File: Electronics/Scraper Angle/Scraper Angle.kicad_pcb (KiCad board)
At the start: 2 copper layers, 43 x 51 mm, 20 parts, among them J1 TERM, J12 SENSOR, J14 CAN BUS, J2 CAN BUS, J3 Conn_01x02, J4 Conn_01x02, J5 Conn_01x02, U1 TJA1462ATK-0Z, U2 PESD2CANFD24V-TR, U3 TEENSY 4.0

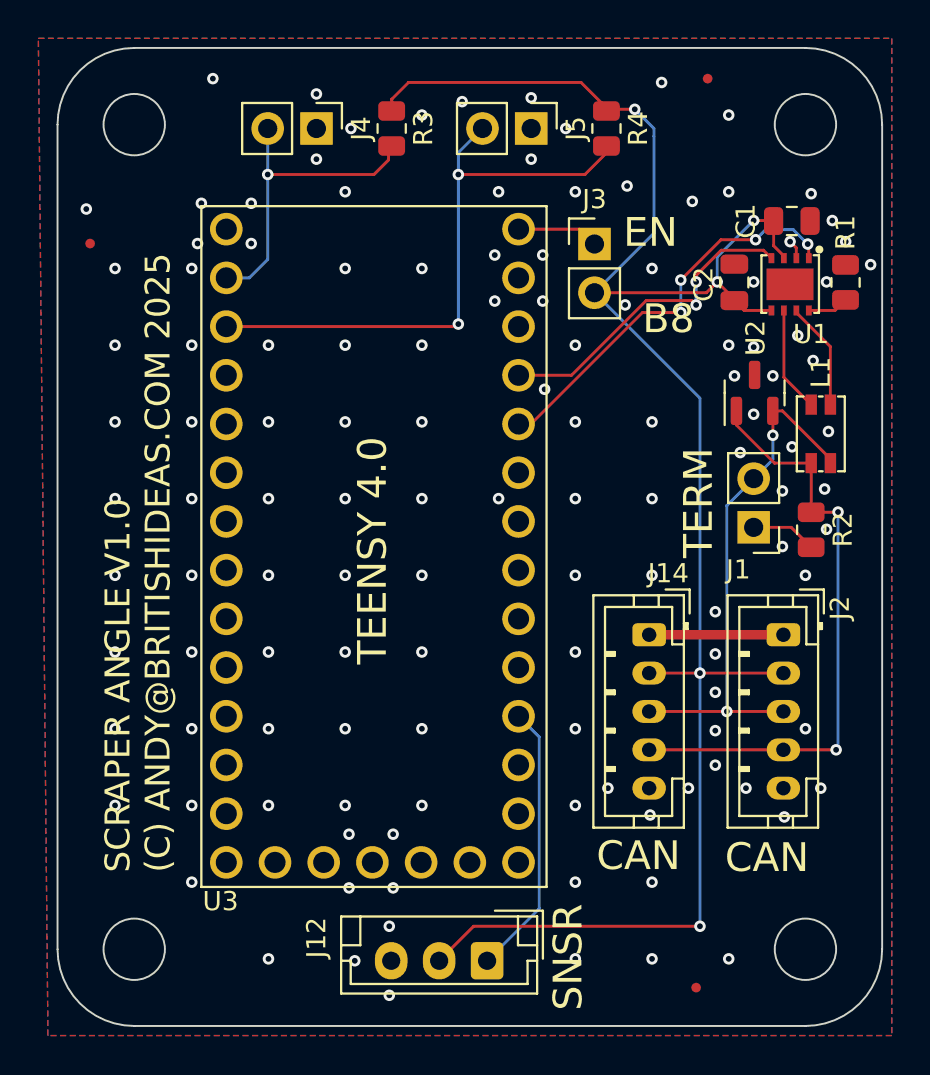
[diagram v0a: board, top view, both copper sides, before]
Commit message: Changed sensor connector on scraper angle board. Generated production files for scraper angle board.
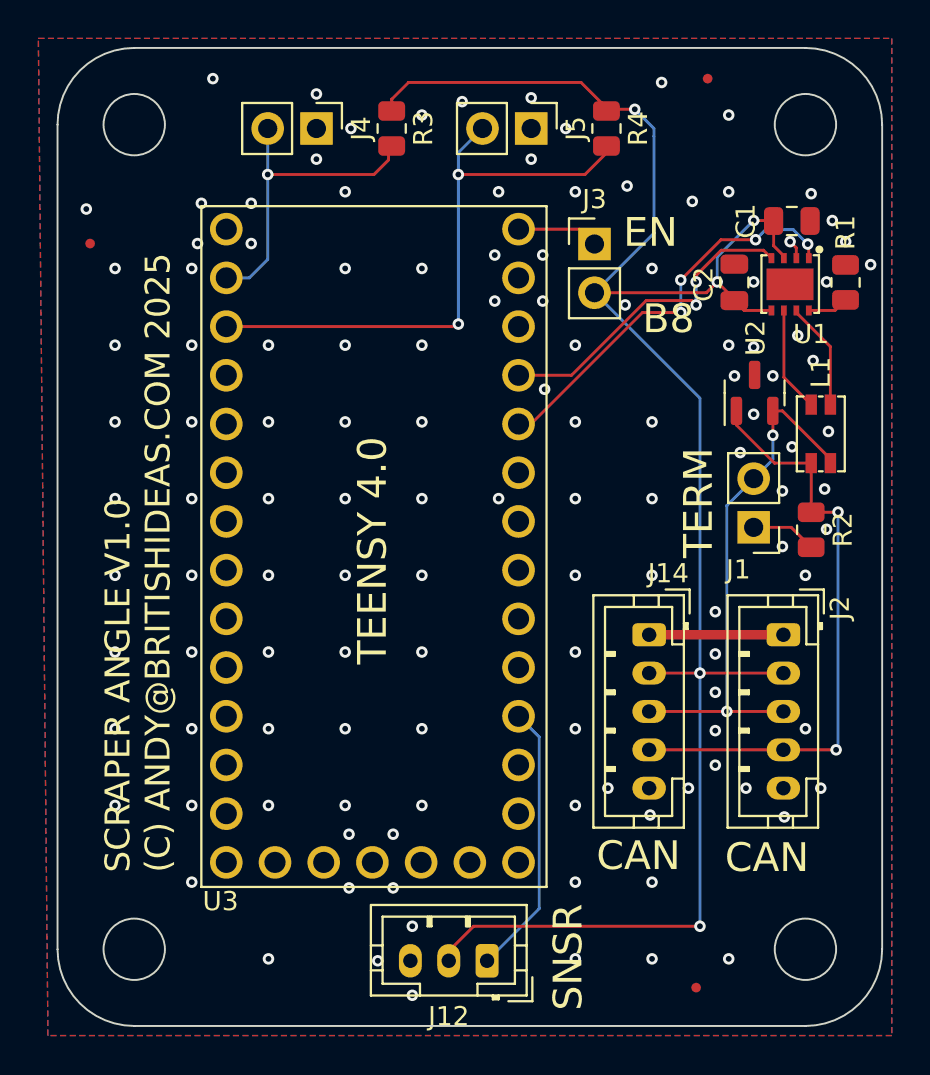
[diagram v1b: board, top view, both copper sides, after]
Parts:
- J12: footprint Connector_JST:JST_EH_B3B-EH-A_1x03_P2.50mm_Vertical -> Connector_JST:JST_PH_B3B-PH-K_1x03_P2.00mm_Vertical
